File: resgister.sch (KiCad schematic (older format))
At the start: 6 parts, among them U1 74LS245, U2 74LS173, U3 74LS173, U4 74LS245, U5 74LS173, U6 74LS173

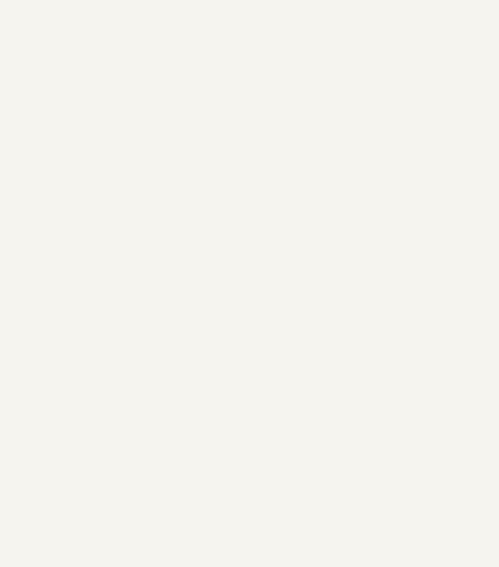
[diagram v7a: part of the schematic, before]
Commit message: added power caps
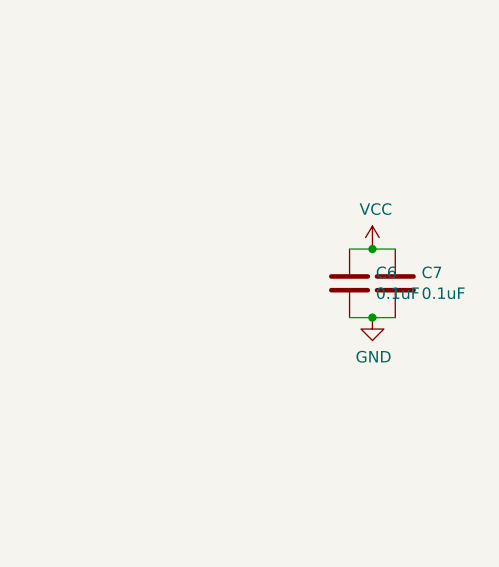
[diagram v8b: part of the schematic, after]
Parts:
- added C8, C9: 0.1uF, Capacitor_THT:CP_Axial_L10.0mm_D4.5mm_P15.00mm_Horizontal, symbol Device:C
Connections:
- net labels added: VCC
- wire segments 277 -> 281
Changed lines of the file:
@@
 AR Path="/5FB94562/61968D37" Ref="#PWR?"  Part="1"
 AR Path="/616D5CDC/61968D37" Ref="#PWR?"  Part="1"
-F 0 "#PWR040" H 2600 4600 50  0001 C CNN
+F 0 "#PWR011" H 2600 4600 50  0001 C CNN
 F 1 "GND" H 2605 4677 50  0000 C CNN
 F 2 "" H 2600 4850 50  0001 C CNN
@@
 AR Path="/5FB94562/61968D38" Ref="#PWR?"  Part="1"
 AR Path="/616D5CDC/61968D38" Ref="#PWR?"  Part="1"
-F 0 "#PWR041" H 3300 3250 50  0001 C CNN
+F 0 "#PWR012" H 3300 3250 50  0001 C CNN
 F 1 "GND" H 3305 3327 50  0000 C CNN
 F 2 "" H 3300 3500 50  0001 C CNN
@@
 AR Path="/5FB94562/61968D39" Ref="#PWR?"  Part="1"
 AR Path="/616D5CDC/61968D39" Ref="#PWR?"  Part="1"
-F 0 "#PWR043" H 4150 3250 50  0001 C CNN
+F 0 "#PWR014" H 4150 3250 50  0001 C CNN
 F 1 "GND" H 4155 3327 50  0000 C CNN
 F 2 "" H 4150 3500 50  0001 C CNN
@@
 AR Path="/5FB94562/5F7355A8" Ref="#PWR?"  Part="1"
 AR Path="/616D5CDC/5F7355A8" Ref="#PWR?"  Part="1"
-F 0 "#PWR047" H 4400 4700 50  0001 C CNN
+F 0 "#PWR018" H 4400 4700 50  0001 C CNN
 F 1 "+5V" H 4415 5023 50  0000 C CNN
 F 2 "" H 4400 4850 50  0001 C CNN
@@
 AR Path="/5FB94562/61968D3C" Ref="#PWR?"  Part="1"
 AR Path="/616D5CDC/61968D3C" Ref="#PWR?"  Part="1"
-F 0 "#PWR049" H 5800 4150 50  0001 C CNN
+F 0 "#PWR020" H 5800 4150 50  0001 C CNN
 F 1 "+5V" H 5815 4473 50  0000 C CNN
 F 2 "" H 5800 4300 50  0001 C CNN
@@
 AR Path="/5FB94562/61968D3D" Ref="#PWR?"  Part="1"
 AR Path="/616D5CDC/61968D3D" Ref="#PWR?"  Part="1"
-F 0 "#PWR062" H 8500 5500 50  0001 C CNN
+F 0 "#PWR033" H 8500 5500 50  0001 C CNN
 F 1 "+5V" H 8515 5823 50  0000 C CNN
 F 2 "" H 8500 5650 50  0001 C CNN
@@
 AR Path="/5FB94562/61968D3E" Ref="#PWR?"  Part="1"
 AR Path="/616D5CDC/61968D3E" Ref="#PWR?"  Part="1"
-F 0 "#PWR063" H 10050 4150 50  0001 C CNN
+F 0 "#PWR034" H 10050 4150 50  0001 C CNN
 F 1 "+5V" H 10065 4473 50  0000 C CNN
 F 2 "" H 10050 4300 50  0001 C CNN
@@
 AR Path="/5FB94562/62492028" Ref="#PWR?"  Part="1"
 AR Path="/616D5CDC/62492028" Ref="#PWR?"  Part="1"
-F 0 "#PWR052" H 5950 3350 50  0001 C CNN
+F 0 "#PWR023" H 5950 3350 50  0001 C CNN
 F 1 "+5V" H 5965 3673 50  0000 C CNN
 F 2 "" H 5950 3500 50  0001 C CNN
@@
 AR Path="/5FB94562/61968D3F" Ref="#PWR?"  Part="1"
 AR Path="/616D5CDC/61968D3F" Ref="#PWR?"  Part="1"
-F 0 "#PWR046" H 4250 2550 50  0001 C CNN
+F 0 "#PWR017" H 4250 2550 50  0001 C CNN
 F 1 "GND" H 4255 2627 50  0000 C CNN
 F 2 "" H 4250 2800 50  0001 C CNN
@@
 AR Path="/5FB94562/61968D34" Ref="#PWR?"  Part="1"
 AR Path="/616D5CDC/61968D34" Ref="#PWR?"  Part="1"
-F 0 "#PWR056" H 7400 4050 50  0001 C CNN
+F 0 "#PWR027" H 7400 4050 50  0001 C CNN
 F 1 "GND" H 7405 4127 50  0000 C CNN
 F 2 "" H 7400 4300 50  0001 C CNN
@@
 AR Path="/5FB94562/616C3790" Ref="#PWR?"  Part="1"
 AR Path="/616D5CDC/616C3790" Ref="#PWR?"  Part="1"
-F 0 "#PWR059" H 8250 4050 50  0001 C CNN
+F 0 "#PWR030" H 8250 4050 50  0001 C CNN
 F 1 "GND" H 8255 4127 50  0000 C CNN
 F 2 "" H 8250 4300 50  0001 C CNN
@@
 AR Path="/5FB94562/616C3791" Ref="#PWR?"  Part="1"
 AR Path="/616D5CDC/616C3791" Ref="#PWR?"  Part="1"
-F 0 "#PWR054" H 6700 5400 50  0001 C CNN
+F 0 "#PWR025" H 6700 5400 50  0001 C CNN
 F 1 "GND" H 6705 5477 50  0000 C CNN
 F 2 "" H 6700 5650 50  0001 C CNN
@@
 AR Path="/5FB94562/62492023" Ref="#PWR?"  Part="1"
 AR Path="/616D5CDC/62492023" Ref="#PWR?"  Part="1"
-F 0 "#PWR044" H 4150 3250 50  0001 C CNN
+F 0 "#PWR015" H 4150 3250 50  0001 C CNN
 F 1 "GND" H 4155 3327 50  0000 C CNN
 F 2 "" H 4150 3500 50  0001 C CNN
@@
 AR Path="/5FB94562/62492019" Ref="#PWR?"  Part="1"
 AR Path="/616D5CDC/62492019" Ref="#PWR?"  Part="1"
-F 0 "#PWR048" H 4400 4700 50  0001 C CNN
+F 0 "#PWR019" H 4400 4700 50  0001 C CNN
 F 1 "+5V" H 4415 5023 50  0000 C CNN
 F 2 "" H 4400 4850 50  0001 C CNN
@@
 AR Path="/5FB94562/6249201A" Ref="#PWR?"  Part="1"
 AR Path="/616D5CDC/6249201A" Ref="#PWR?"  Part="1"
-F 0 "#PWR050" H 5800 4150 50  0001 C CNN
+F 0 "#PWR021" H 5800 4150 50  0001 C CNN
 F 1 "+5V" H 5815 4473 50  0000 C CNN
 F 2 "" H 5800 4300 50  0001 C CNN
@@
 AR Path="/5FB94562/61968D24" Ref="#PWR?"  Part="1"
 AR Path="/616D5CDC/61968D24" Ref="#PWR?"  Part="1"
-F 0 "#PWR061" H 8500 5500 50  0001 C CNN
+F 0 "#PWR032" H 8500 5500 50  0001 C CNN
 F 1 "+5V" H 8515 5823 50  0000 C CNN
 F 2 "" H 8500 5650 50  0001 C CNN
@@
 AR Path="/5FB94562/6249201B" Ref="#PWR?"  Part="1"
 AR Path="/616D5CDC/6249201B" Ref="#PWR?"  Part="1"
-F 0 "#PWR064" H 10050 4150 50  0001 C CNN
+F 0 "#PWR035" H 10050 4150 50  0001 C CNN
 F 1 "+5V" H 10065 4473 50  0000 C CNN
 F 2 "" H 10050 4300 50  0001 C CNN
@@
 AR Path="/5FB94562/616C37AD" Ref="#PWR?"  Part="1"
 AR Path="/616D5CDC/616C37AD" Ref="#PWR?"  Part="1"
-F 0 "#PWR057" H 7800 3400 50  0001 C CNN
+F 0 "#PWR028" H 7800 3400 50  0001 C CNN
 F 1 "GND" H 7805 3477 50  0000 C CNN
 F 2 "" H 7800 3650 50  0001 C CNN
@@
 AR Path="/5FB94562/61968D30" Ref="#PWR?"  Part="1"
 AR Path="/616D5CDC/61968D30" Ref="#PWR?"  Part="1"
-F 0 "#PWR037" H 1700 3350 50  0001 C CNN
+F 0 "#PWR08" H 1700 3350 50  0001 C CNN
 F 1 "+5V" H 1715 3673 50  0000 C CNN
 F 2 "" H 1700 3500 50  0001 C CNN
@@
 Wire Wire Line
 	5250 6850 10550 6850
+$Comp
+L 16bitCpu-rescue:VCC-power #PWR?
+U 1 1 5FB15BC2
+P 11950 2400
+AR Path="/5FB15BC2" Ref="#PWR?"  Part="1"
+AR Path="/5F74778C/5FB15BC2" Ref="#PWR0188"  Part="1"
+AR Path="/5F67C726/5FB15BC2" Ref="#PWR0110"  Part="1"
+F 0 "#PWR0110" H 11950 2250 50  0001 C CNN
+F 1 "VCC" H 11965 2573 50  0000 C CNN
+F 2 "" H 11950 2400 50  0001 C CNN
+F 3 "" H 11950 2400 50  0001 C CNN
+	1    11950 2400
+	1    0    0    -1
+$EndComp
+$Comp
+L 16bitCpu-rescue:GND-power #PWR?
+U 1 1 5FB15BC8
+P 11950 2700
+AR Path="/5FB15BC8" Ref="#PWR?"  Part="1"
+AR Path="/5F75E433/5FB15BC8" Ref="#PWR?"  Part="1"
+AR Path="/5F74778C/5FB15BC8" Ref="#PWR0262"  Part="1"
+AR Path="/5F67C726/5FB15BC8" Ref="#PWR0111"  Part="1"
+F 0 "#PWR0111" H 11950 2450 50  0001 C CNN
+F 1 "GND" H 11955 2527 50  0000 C CNN
+F 2 "" H 11950 2700 50  0001 C CNN
+F 3 "" H 11950 2700 50  0001 C CNN
+	1    11950 2700
+	1    0    0    -1
+$EndComp
+Wire Wire Line
+	11950 2400 12050 2400
+Wire Wire Line
+	12050 2700 11950 2700
+$Comp
+L Device:C C?
+U 1 1 5FB15BD0
+P 11850 2550
+AR Path="/5F75E433/5FB15BD0" Ref="C?"  Part="1"
+AR Path="/5F74778C/5FB15BD0" Ref="C8"  Part="1"
+AR Path="/5F67C726/5FB15BD0" Ref="C6"  Part="1"
+F 0 "C6" H 11965 2596 50  0000 L CNN
+F 1 "0.1uF" H 11965 2505 50  0000 L CNN
+F 2 "Capacitor_THT:CP_Axial_L10.0mm_D4.5mm_P15.00mm_Horizontal" H 11888 2400 50  0001 C CNN
+F 3 "" H 11850 2550 50  0001 C CNN
+	1    11850 2550
+	1    0    0    -1
+$EndComp
+Wire Wire Line
+	11950 2400 11850 2400
+Connection ~ 11950 2400
+Wire Wire Line
+	11850 2700 11950 2700
+Connection ~ 11950 2700
+$Comp
+L Device:C C?
+U 1 1 5FB15BDA
+P 12050 2550
+AR Path="/5F75E433/5FB15BDA" Ref="C?"  Part="1"
+AR Path="/5F74778C/5FB15BDA" Ref="C9"  Part="1"
+AR Path="/5F67C726/5FB15BDA" Ref="C7"  Part="1"
+F 0 "C7" H 12165 2596 50  0000 L CNN
+F 1 "0.1uF" H 12165 2505 50  0000 L CNN
+F 2 "Capacitor_THT:CP_Axial_L10.0mm_D4.5mm_P15.00mm_Horizontal" H 12088 2400 50  0001 C CNN
+F 3 "" H 12050 2550 50  0001 C CNN
+	1    12050 2550
+	1    0    0    -1
+$EndComp
 $EndSCHEMATC
